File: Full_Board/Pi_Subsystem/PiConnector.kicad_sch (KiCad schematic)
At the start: 4 parts

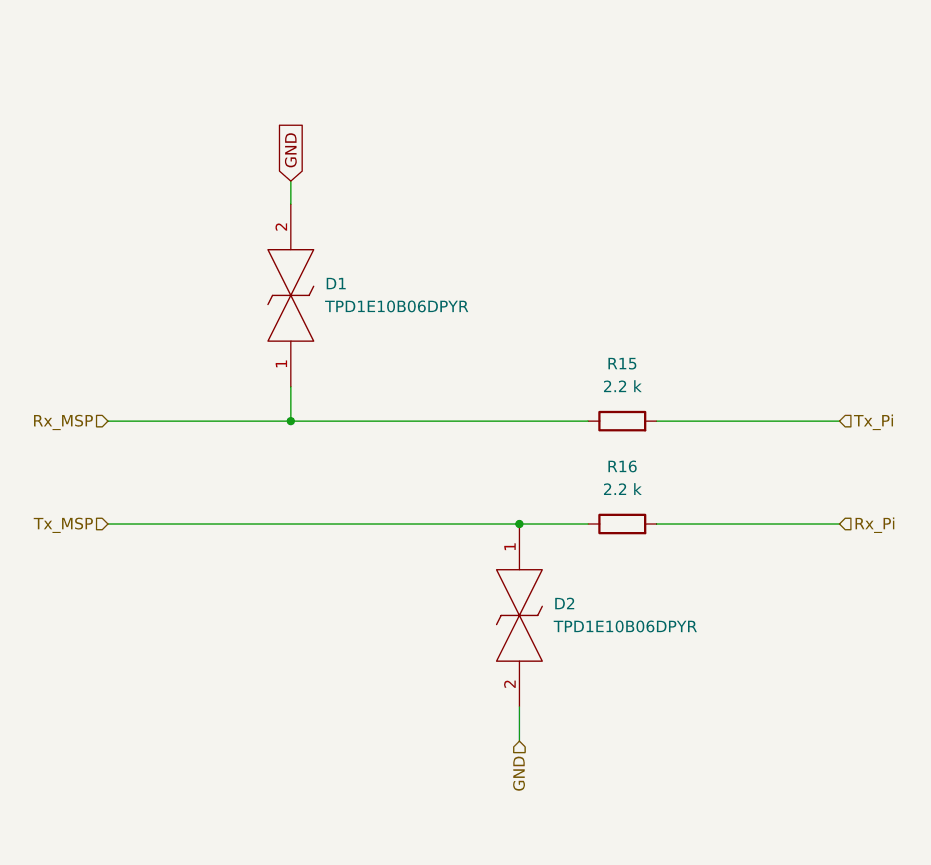
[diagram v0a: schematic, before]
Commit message: Adjusted the Pi subsystem
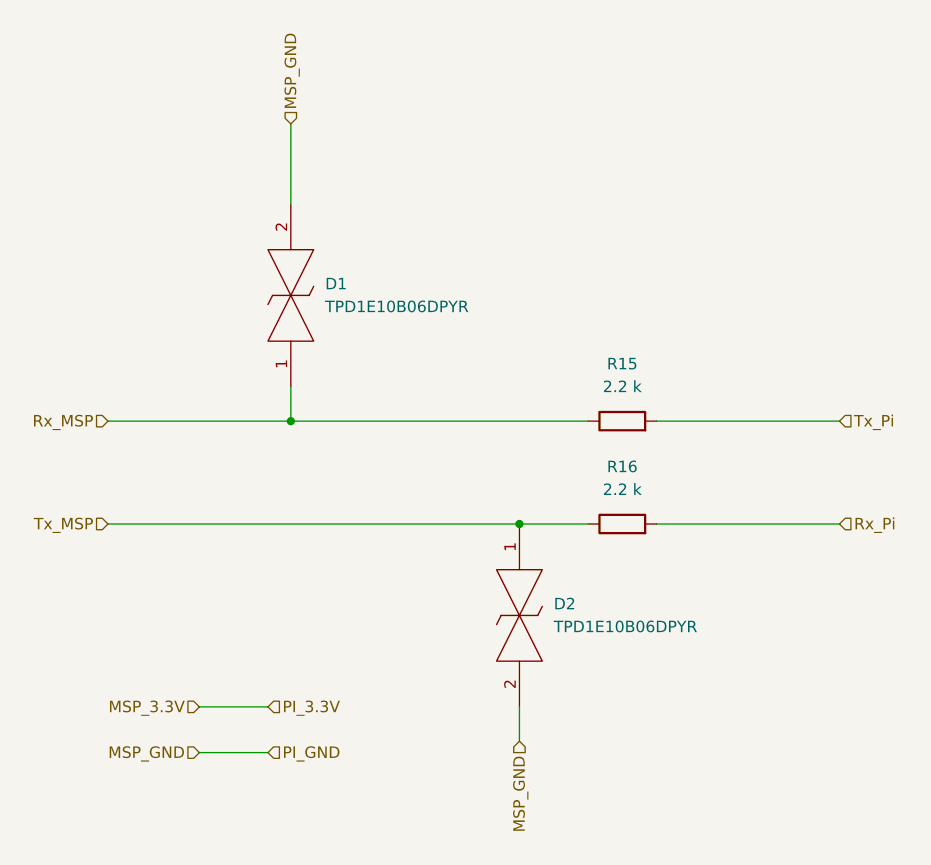
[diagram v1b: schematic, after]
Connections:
- net GND renamed MSP_GND
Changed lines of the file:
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@@
     (stroke (width 0) (type default) (color 0 0 0 0))
   )
-  (wire (pts (xy 127 64.77) (xy 127 67.31))
+  (wire (pts (xy 127 58.42) (xy 127 67.31))
+    (stroke (width 0) (type default) (color 0 0 0 0))
+  )
+  (wire (pts (xy 116.84 123.19) (xy 124.46 123.19))
     (stroke (width 0) (type default) (color 0 0 0 0))
   )
   (wire (pts (xy 167.64 91.44) (xy 187.96 91.44))
+    (stroke (width 0) (type default) (color 0 0 0 0))
+  )
+  (wire (pts (xy 116.84 128.27) (xy 124.46 128.27))
     (stroke (width 0) (type default) (color 0 0 0 0))
   )
@@
     (stroke (width 0) (type default) (color 0 0 0 0))
   )
-  (global_label "GND" (shape input) (at 127 64.77 90) (fields_autoplaced)
-    (effects (font (size 1.27 1.27)) (justify left))
-    (property "Intersheet References" "${INTERSHEET_REFS}" (id 0) (at 126.9206 58.4864 90)
-      (effects (font (size 1.27 1.27)) (justify left) hide)
-    )
-  )
-  (hierarchical_label "GND" (shape input) (at 152.4 127 270)
+  (hierarchical_label "MSP_GND" (shape input) (at 152.4 127 270)
     (effects (font (size 1.27 1.27)) (justify right))
   )
@@
     (effects (font (size 1.27 1.27)) (justify left))
   )
+  (hierarchical_label "MSP_GND" (shape input) (at 116.84 128.27 180)
+    (effects (font (size 1.27 1.27)) (justify right))
+  )
   (hierarchical_label "Rx_MSP" (shape input) (at 106.68 91.44 180)
     (effects (font (size 1.27 1.27)) (justify right))
   )
+  (hierarchical_label "PI_GND" (shape input) (at 124.46 128.27 0)
+    (effects (font (size 1.27 1.27)) (justify left))
+  )
   (hierarchical_label "Rx_Pi" (shape input) (at 187.96 102.87 0)
+    (effects (font (size 1.27 1.27)) (justify left))
+  )
+  (hierarchical_label "PI_3.3V" (shape input) (at 124.46 123.19 0)
     (effects (font (size 1.27 1.27)) (justify left))
   )
@@
     (effects (font (size 1.27 1.27)) (justify right))
   )
+  (hierarchical_label "MSP_3.3V" (shape input) (at 116.84 123.19 180)
+    (effects (font (size 1.27 1.27)) (justify right))
+  )
+  (hierarchical_label "MSP_GND" (shape input) (at 127 58.42 90)
+    (effects (font (size 1.27 1.27)) (justify left))
+  )
   (symbol (lib_id "Device:R") (at 163.83 91.44 90) (unit 1)

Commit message: Add screenshots of each subsystem
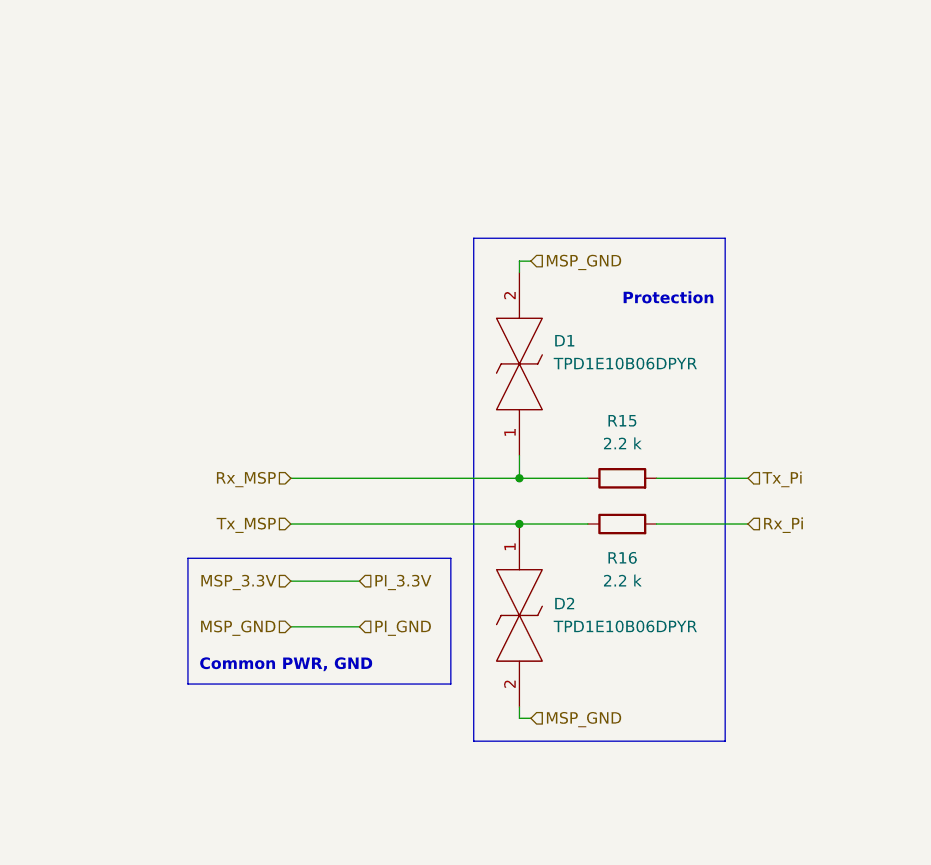
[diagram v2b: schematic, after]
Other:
- note added: "Common PWR, GND"
- note added: "Protection"
- moved on the sheet: D1, R15

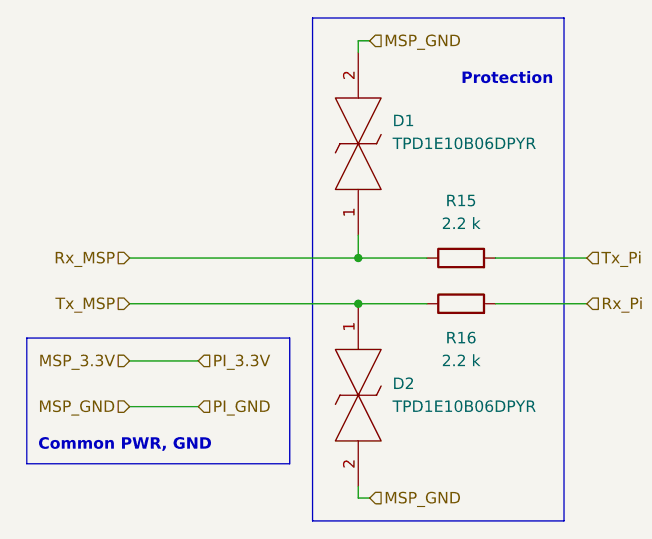
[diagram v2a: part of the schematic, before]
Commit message: Added a fuse and fixed ERC
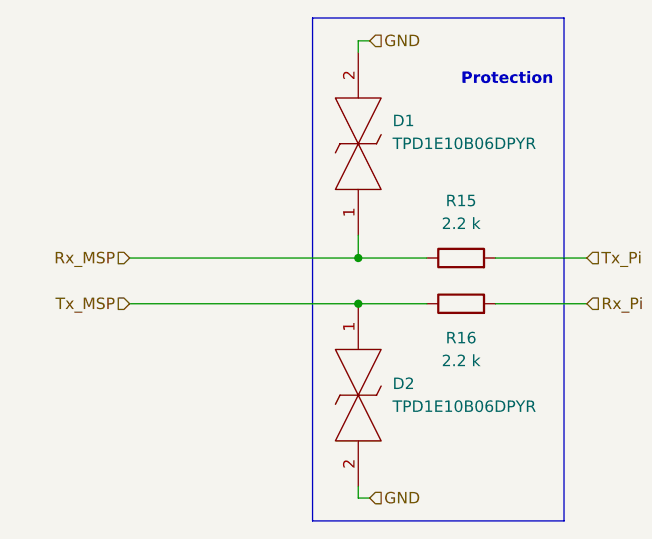
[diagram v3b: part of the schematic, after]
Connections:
- net MSP_GND renamed GND
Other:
- note removed: "Common PWR, GND"
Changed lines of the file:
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@@
-    (stroke (width 0) (type default) (color 0 0 0 0))
-  )
-  (wire (pts (xy 127 109.22) (xy 134.62 109.22))
     (stroke (width 0) (type default) (color 0 0 0 0))
   )
@@
     (stroke (width 0) (type default) (color 0 0 0 0))
   )
-  (wire (pts (xy 127 114.3) (xy 134.62 114.3))
-    (stroke (width 0) (type default) (color 0 0 0 0))
-  )
   (wire (pts (xy 152.4 95.25) (xy 152.4 97.79))
     (stroke (width 0) (type default) (color 0 0 0 0))
   )
-  (polyline (pts (xy 144.78 120.65) (xy 115.57 120.65))
-    (stroke (width 0) (type default) (color 0 0 0 0))
-  )
   (wire (pts (xy 152.4 97.79) (xy 160.02 97.79))
-    (stroke (width 0) (type default) (color 0 0 0 0))
-  )
-  (polyline (pts (xy 144.78 106.68) (xy 144.78 120.65))
     (stroke (width 0) (type default) (color 0 0 0 0))
   )
@@
     (stroke (width 0) (type default) (color 0 0 0 0))
   )
-  (polyline (pts (xy 115.57 106.68) (xy 144.78 106.68))
-    (stroke (width 0) (type default) (color 0 0 0 0))
-  )
   (wire (pts (xy 167.64 102.87) (xy 177.8 102.87))
-    (stroke (width 0) (type default) (color 0 0 0 0))
-  )
-  (polyline (pts (xy 115.57 120.65) (xy 115.57 106.68))
     (stroke (width 0) (type default) (color 0 0 0 0))
   )
@@
     (effects (font (size 1.27 1.27) bold) (justify left bottom))
   )
-  (text "Common PWR, GND" (at 116.84 119.38 0)
-    (effects (font (size 1.27 1.27) bold) (justify left bottom))
-  )
-  (hierarchical_label "MSP_GND" (shape input) (at 153.67 124.46 0)
+  (hierarchical_label "GND" (shape input) (at 153.67 124.46 0)
     (effects (font (size 1.27 1.27)) (justify left))
   )
@@
     (effects (font (size 1.27 1.27)) (justify left))
   )
-  (hierarchical_label "MSP_GND" (shape input) (at 127 114.3 180)
-    (effects (font (size 1.27 1.27)) (justify right))
-  )
   (hierarchical_label "Rx_MSP" (shape input) (at 127 97.79 180)
     (effects (font (size 1.27 1.27)) (justify right))
   )
-  (hierarchical_label "PI_GND" (shape input) (at 134.62 114.3 0)
-    (effects (font (size 1.27 1.27)) (justify left))
-  )
   (hierarchical_label "Rx_Pi" (shape input) (at 177.8 102.87 0)
-    (effects (font (size 1.27 1.27)) (justify left))
-  )
-  (hierarchical_label "PI_3.3V" (shape input) (at 134.62 109.22 0)
     (effects (font (size 1.27 1.27)) (justify left))
   )
@@
     (effects (font (size 1.27 1.27)) (justify right))
   )
-  (hierarchical_label "MSP_3.3V" (shape input) (at 127 109.22 180)
-    (effects (font (size 1.27 1.27)) (justify right))
-  )
-  (hierarchical_label "MSP_GND" (shape input) (at 153.67 73.66 0)
+  (hierarchical_label "GND" (shape input) (at 153.67 73.66 0)
     (effects (font (size 1.27 1.27)) (justify left))
   )
